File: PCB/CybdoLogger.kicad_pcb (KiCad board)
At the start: 2 copper layers, 16 x 50 mm, 33 parts, among them SW2 READ, U1 RP2040, U2 USBLC6-2SC6, U3 USBLC6-2SC6, U4 MCP1700x-330xxTT, U5 W25Q16JVUXIQ, Y1 Crystal_GND24

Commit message: mroe rounting
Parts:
- added C16: 100nF, Capacitor_SMD:C_0402_1005Metric, F.Cu at (65.3, 86.0)
- added C17: 10uF, Capacitor_SMD:C_0402_1005Metric, F.Cu at (65.3, 87.9)
- added R6: 10kR, Resistor_SMD:R_0402_1005Metric, F.Cu at (62.4, 86.0)
- added R7: 10kR, Resistor_SMD:R_0402_1005Metric, F.Cu at (62.4, 88.0)
- USB1: moved to B.Cu
- moved SW2 96.5 mm to (46.5, 62.0)
- moved C2 96.2 mm to (43.3, 55.8), turned to 90 degrees
- moved C13 94.0 mm to (47.0, 77.2)
- moved C10 91.9 mm to (49.2, 65.1), turned to -90 degrees
- moved R3 91.6 mm to (46.3, 75.5), turned to 90 degrees
- moved C1 91.4 mm to (47.4, 56.8), turned to -90 degrees
- moved C8 90.1 mm to (48.3, 76.2), turned to 135 degrees
- moved C9 86.1 mm to (54.7, 65.0), turned to -45 degrees
- moved C7 85.8 mm to (53.5, 67.5), turned to -135 degrees
- moved Y1 84.9 mm to (44.1, 76.0), turned to 90 degrees
- moved R1 84.2 mm to (54.3, 54.7), turned to -135 degrees
- moved R2 82.6 mm to (55.8, 57.7)
- moved C4 79.6 mm to (44.1, 78.7)
- moved C11 69.0 mm to (69.2, 85.8)
- moved C12 69.0 mm to (69.2, 87.7)
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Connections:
- U1 pad 2: unconnected-(U1-GPIO0-Pad2) -> /READ_SD
- U2 pad 1: /UD+ -> /UD-
- U2 pad 3: /UD- -> /UD+
- U2 pad 4: /USB_UP_D- -> /USB_UP_D+
- U2 pad 6: /USB_UP_D+ -> /USB_UP_D-
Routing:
- net +3V3: track 13.3 -> 64.9 mm, vias 2 -> 9
- net /UD-: track 25.2 -> 3.98 mm
- net /UD+: track 24.3 -> 4.09 mm
- net VBUS: track 2.21 -> 17.9 mm
- net +1V1: track 3.23 -> 16.7 mm, vias 0 -> 1
- net /USB_UP_D-: track 2.32 -> 15.8 mm
- net /BOOTSEL: track 4.55 -> 17.3 mm, vias 0 -> 2
- net GND: track 0.44 -> 11.9 mm, vias 2 -> 28
- net /USB_UP_D+: track 4.38 -> 15.8 mm
- net /FLASH_SD2: track 3.11 -> 10.4 mm, vias 0 -> 2
- net /SD_CD: track 0.00 -> 6.17 mm, vias 0 -> 1
- net /READ_SD: track 0.00 -> 5.37 mm
- net Net-(U1-XIN): track 0.00 -> 4.89 mm
- net /FLASH_SD1: track 4.91 -> 9.35 mm
- net Net-(C4-Pad2): track 0.00 -> 3.57 mm
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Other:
- board size 16 x 50 mm -> 16 x 45 mm

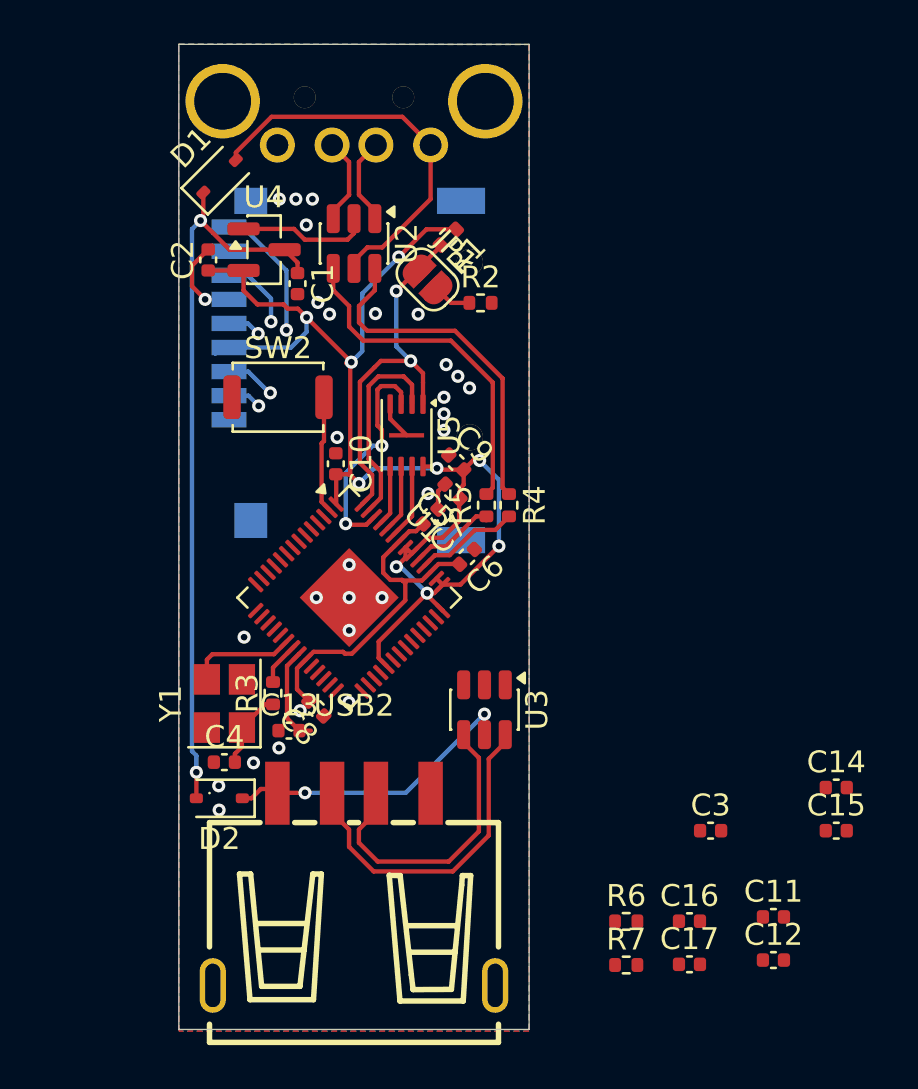
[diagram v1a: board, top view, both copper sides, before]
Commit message: nearly done routing
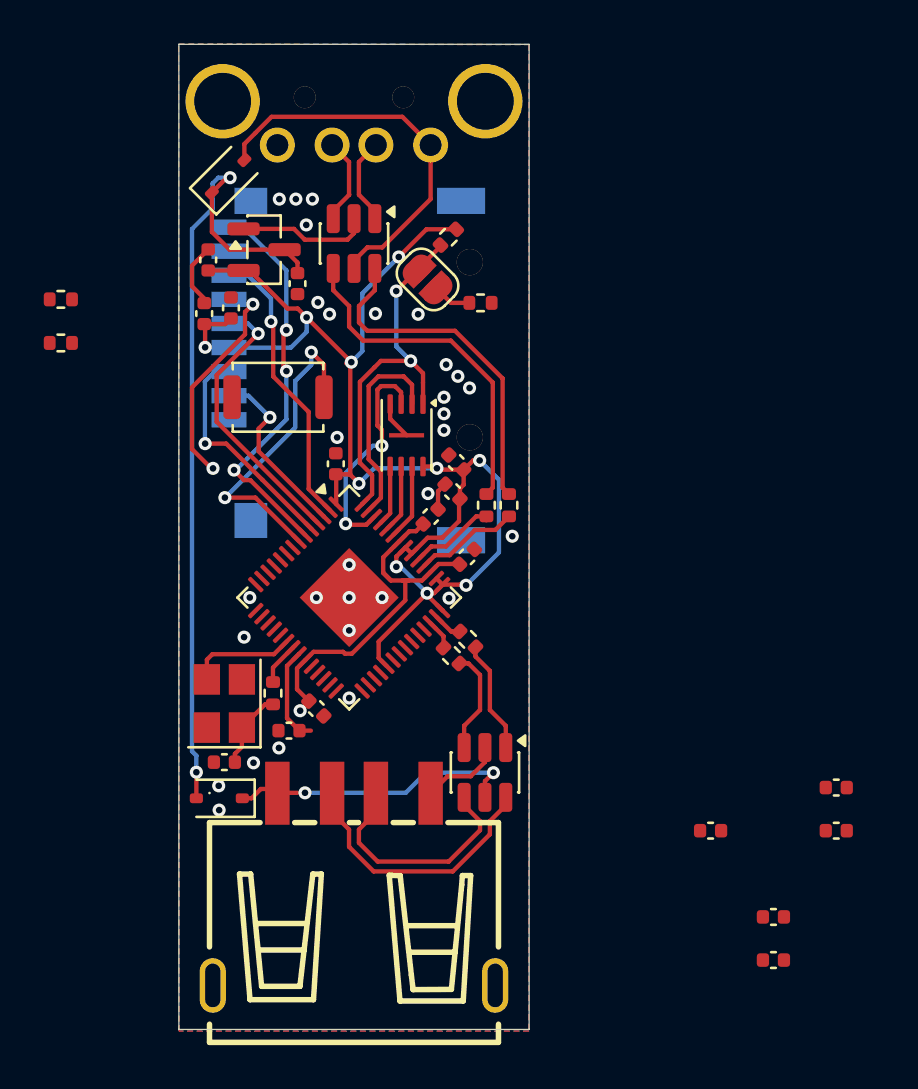
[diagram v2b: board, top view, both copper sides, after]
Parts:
- added R8: 27R, Resistor_SMD:R_0402_1005Metric, F.Cu at (54.5, 73.8)
- added R9: 27R, Resistor_SMD:R_0402_1005Metric, F.Cu at (55.2, 73.1)
- moved R6 38.4 mm to (36.6, 57.5)
- moved R7 38.4 mm to (36.6, 59.5)
- moved C17 36.6 mm to (44.4, 57.9), turned to -90 degrees
- moved C16 35.5 mm to (43.2, 58.2), turned to -90 degrees
- moved U3 2.87 mm to (56.0, 79.2)
- moved D1 0.39 mm to (44.2, 51.9)
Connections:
- U1 pad 2: /READ_SD -> /SD_MISO
- U1 pad 3: unconnected-(U1-GPIO1-Pad3) -> /SD_CS
- U1 pad 4: unconnected-(U1-GPIO2-Pad4) -> /SD_CLK
- U1 pad 40: unconnected-(U1-GPIO28/ADC2-Pad40) -> Net-(U1-GPIO28/ADC2)
- U1 pad 41: unconnected-(U1-GPIO29/ADC3-Pad41) -> Net-(U1-GPIO29/ADC3)
- U1 pad 5: unconnected-(U1-GPIO3-Pad5) -> /SD_MOSI
- U1 pad 6: unconnected-(U1-GPIO4-Pad6) -> /SD_CD
- U1 pad 7: unconnected-(U1-GPIO5-Pad7) -> /READ_SD
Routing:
- net GND: track 11.9 -> 24.7 mm, vias 28 -> 32
- net /SD_CD: track 6.17 -> 18.2 mm, vias 1 -> 3
- net /SD_CLK: track 2.17 -> 13.5 mm
- net /SD_MISO: track 3.42 -> 13.2 mm
- net /READ_SD: track 5.37 -> 14.8 mm, vias 0 -> 2
- net /SD_MOSI: track 2.29 -> 10.6 mm
- net /SD_CS: track 1.55 -> 8.26 mm
- net /USB_DOWN_D-: track 0.00 -> 5.15 mm
- net /USB_DOWN_D+: track 0.00 -> 4.78 mm
- net VSYS: track 33.7 -> 37.4 mm
- net /DD-: track 15.6 -> 12.4 mm
- net +3V3: track 64.9 -> 67.9 mm, vias 9 -> 10
- net /DD+: track 13.7 -> 10.9 mm
- net Net-(U1-GPIO28/ADC2): track 0.00 -> 1.38 mm
- net Net-(U1-GPIO29/ADC3): track 0.00 -> 1.34 mm
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
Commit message: polishing
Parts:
- moved C14 29.3 mm to (45.2, 68.0), turned to -45 degrees
- moved C3 24.5 mm to (43.5, 72.9), turned to -90 degrees
- moved C12 22.2 mm to (56.2, 69.7), turned to -135 degrees
- moved C15 20.3 mm to (53.0, 74.6), turned to -135 degrees
- moved C11 18.8 mm to (55.9, 72.3), turned to 135 degrees
- moved R6 12.7 mm to (47.4, 64.2)
- moved R7 9.64 mm to (43.0, 66.8), turned to -90 degrees
- moved C1 4.97 mm to (48.1, 51.9), turned to 135 degrees
- moved C2 4.19 mm to (47.5, 56.3), turned to -45 degrees
- moved U4 1.67 mm to (46.3, 53.7), turned to 45 degrees
- moved C16 0.31 mm to (43.3, 57.9)
- moved C10 0.06 mm to (49.2, 65.0)
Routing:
- net +3V3: track 67.9 -> 94.1 mm, vias 10 -> 8
- net GND: track 24.7 -> 33.6 mm, vias 32 -> 33
- net /READ_SD: track 14.8 -> 8.24 mm
- net unconnected-(Card1-DAT2-Pad1): track 0.00 -> 5.72 mm
- net unconnected-(Card1-DAT1-Pad8): track 0.00 -> 2.48 mm, vias 0 -> 1
- net /BOOTSEL: track 17.3 -> 19.7 mm
- net /SD_MOSI: track 10.6 -> 13.0 mm
- net VSYS: track 37.4 -> 35.7 mm
- net Net-(U1-XIN): track 4.89 -> 5.76 mm
- net /SD_CLK: track 13.5 -> 12.9 mm
- net /SD_CD: track 18.2 -> 18.7 mm, vias 3 -> 1
- net +1V1: track 17.2 -> 17.0 mm, vias 1 -> 0

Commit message: pcb done
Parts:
- added R10: 10kR, Resistor_SMD:R_0402_1005Metric, F.Cu at (44.5, 69.4)
- added R11: 10kR, Resistor_SMD:R_0402_1005Metric, F.Cu at (47.6, 59.7)
- moved C1 5.15 mm to (44.1, 55.1)
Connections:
- Card1 pad 1: unconnected-(Card1-DAT2-Pad1) -> /SD_DAT0
- Card1 pad 8: unconnected-(Card1-DAT1-Pad8) -> /SD_DAT1
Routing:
- net GND: track 33.6 -> 42.4 mm, vias 33 -> 35
- net /SD_DAT0: track 0.00 -> 7.73 mm, vias 0 -> 1
- net /SD_DAT1: track 0.00 -> 6.49 mm, vias 0 -> 1
- net unconnected-(Card1-DAT2-Pad1): track 5.72 -> 0.00 mm
- net /BOOTSEL: track 19.7 -> 16.4 mm
- net /FLASH_SD2: track 10.2 -> 7.66 mm, vias 2 -> 0
- net unconnected-(Card1-DAT1-Pad8): track 2.48 -> 0.00 mm, vias 1 -> 0
- net +3V3: track 94.1 -> 95.9 mm
- net VSYS: track 35.7 -> 37.4 mm
- net +1V1: track 17.0 -> 15.6 mm
- net /DD-: track 12.4 -> 11.1 mm
- net /DD+: track 10.9 -> 9.62 mm
- net /SD_MOSI: track 13.0 -> 12.3 mm
- net /SD_CLK: track 12.9 -> 12.2 mm
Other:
- board text added: "nothing to see here..."
